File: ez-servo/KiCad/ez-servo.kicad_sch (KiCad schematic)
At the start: 15 parts, among them J1 Driver Pins, J2 SERVO, J3 VSEL, U1 TPS5430DDA

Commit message: fix: add silkscreen markings
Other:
- title: (none) -> EZ Servo
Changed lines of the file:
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@@
 	(generator_version "8.0")
 	(paper "A4")
+	(title_block
+		(title "EZ Servo")
+		(comment 1 "creativecommons.org/licenses/by-sa/4.0/")
+		(comment 2 "License: CC BY-SA 4.0")
+		(comment 3 "Author: Michael Smith")
+	)
 	(junction
 		(at 95.25 143.51)

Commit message: fix: switch feedback resistor footprints for flexibility
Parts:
- R1, R2, R3: footprint Resistor_SMD:R_0805_2012Metric -> Resistor_SMD:R_0805_2012Metric_Pad1.20x1.40mm_HandSolder
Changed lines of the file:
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@@
 			)
 		)
-		(property "Footprint" "Resistor_SMD:R_0805_2012Metric"
+		(property "Footprint" "Resistor_SMD:R_0805_2012Metric_Pad1.20x1.40mm_HandSolder"
 			(at 147.828 124.46 90)
 			(effects
@@
 			)
 		)
-		(property "Footprint" "Resistor_SMD:R_0805_2012Metric"
+		(property "Footprint" "Resistor_SMD:R_0805_2012Metric_Pad1.20x1.40mm_HandSolder"
 			(at 143.002 139.7 90)
 			(effects
@@
 			)
 		)
-		(property "Footprint" "Resistor_SMD:R_0805_2012Metric"
+		(property "Footprint" "Resistor_SMD:R_0805_2012Metric_Pad1.20x1.40mm_HandSolder"
 			(at 156.718 124.46 90)
 			(effects

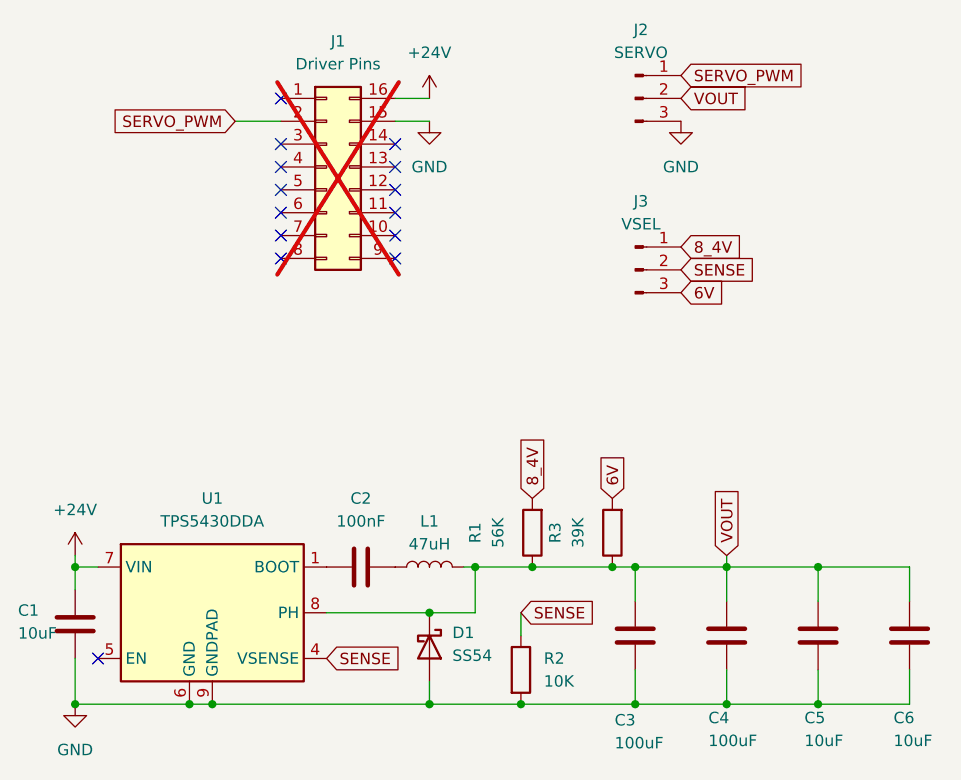
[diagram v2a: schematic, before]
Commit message: feat: add optional servo output through stepper port
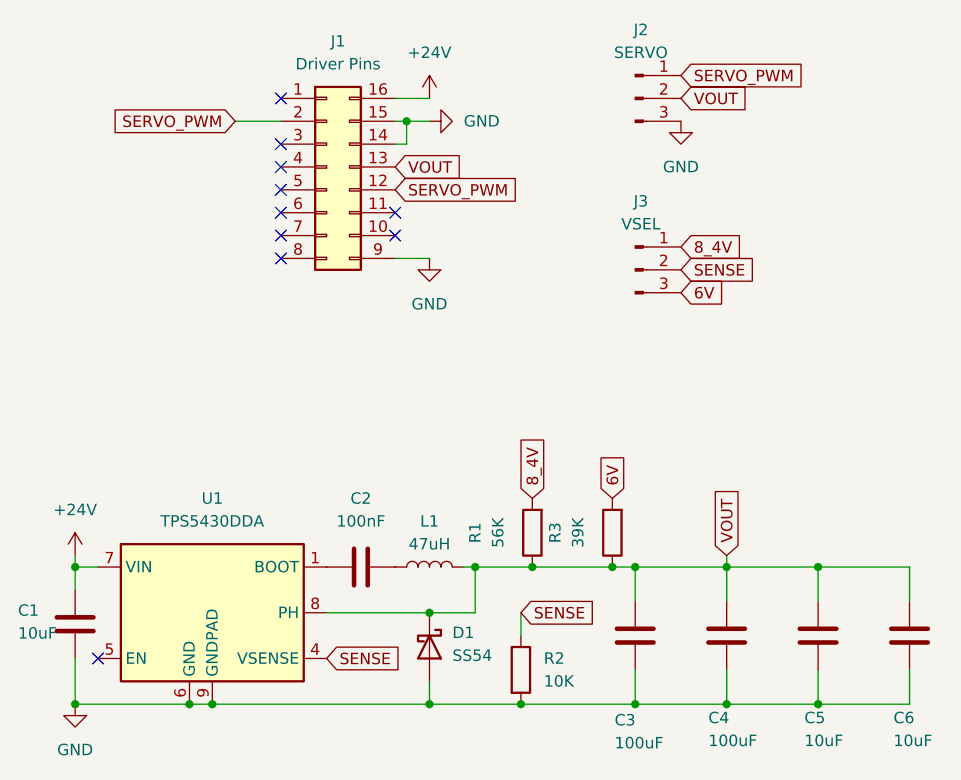
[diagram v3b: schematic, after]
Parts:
- J1: footprint (none) -> Local Library:BTT EZ; now fitted
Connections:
- net GND: now also J1.14 (Pin_14), J1.9 (Pin_9)
- net SERVO_PWM: now also J1.12 (Pin_12)
- net VOUT: now also J1.13 (Pin_13)
- no-connect marks 14 -> 10
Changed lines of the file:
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@@
+	)
+	(junction
+		(at 132.08 78.74)
+		(diameter 0)
+		(color 0 0 0 0)
 	)
 	(junction
@@
 	)
 	(no_connect
-		(at 130.81 83.82)
-	)
-	(no_connect
 		(at 118.11 83.82)
-	)
-	(no_connect
-		(at 130.81 93.98)
 	)
 	(no_connect
@@
 	)
 	(no_connect
-		(at 130.81 81.28)
-	)
-	(no_connect
 		(at 97.79 138.43)
 	)
@@
 	)
 	(no_connect
-		(at 130.81 86.36)
-	)
-	(no_connect
 		(at 118.11 91.44)
 	)
@@
 	(wire
 		(pts
+			(xy 132.08 78.74) (xy 134.62 78.74)
+		)
+		(stroke
+			(width 0)
+			(type default)
+		)
+	)
+	(wire
+		(pts
+			(xy 132.08 81.28) (xy 132.08 78.74)
+		)
+		(stroke
+			(width 0)
+			(type default)
+		)
+	)
+	(wire
+		(pts
 			(xy 95.25 143.51) (xy 107.95 143.51)
 		)
@@
 	(wire
 		(pts
-			(xy 130.81 78.74) (xy 134.62 78.74)
+			(xy 130.81 78.74) (xy 132.08 78.74)
 		)
 		(stroke
@@
 	(wire
 		(pts
+			(xy 130.81 93.98) (xy 134.62 93.98)
+		)
+		(stroke
+			(width 0)
+			(type default)
+		)
+	)
+	(wire
+		(pts
 			(xy 157.48 139.7) (xy 157.48 143.51)
 		)
@@
 	(wire
 		(pts
+			(xy 130.81 81.28) (xy 132.08 81.28)
+		)
+		(stroke
+			(width 0)
+			(type default)
+		)
+	)
+	(wire
+		(pts
 			(xy 95.25 128.27) (xy 95.25 130.81)
 		)
@@
 			(width 0)
 			(type default)
+		)
+	)
+	(global_label "SERVO_PWM"
+		(shape input)
+		(at 130.81 86.36 0)
+		(fields_autoplaced yes)
+		(effects
+			(font
+				(size 1.27 1.27)
+			)
+			(justify left)
+		)
+		(property "Intersheetrefs" "${INTERSHEET_REFS}"
+			(at 144.9832 86.36 0)
+			(effects
+				(font
+					(size 1.27 1.27)
+				)
+				(justify left)
+				(hide yes)
+			)
 		)
 	)
@@
 		(property "Intersheetrefs" "${INTERSHEET_REFS}"
 			(at 154.94 115.3667 90)
+			(effects
+				(font
+					(size 1.27 1.27)
+				)
+				(justify left)
+				(hide yes)
+			)
+		)
+	)
+	(global_label "VOUT"
+		(shape input)
+		(at 130.81 83.82 0)
+		(fields_autoplaced yes)
+		(effects
+			(font
+				(size 1.27 1.27)
+			)
+			(justify left)
+		)
+		(property "Intersheetrefs" "${INTERSHEET_REFS}"
+			(at 138.5124 83.82 0)
 			(effects
 				(font
@@
 		(exclude_from_sim no)
 		(in_bom yes)
-		(on_board no)
-		(dnp yes)
+		(on_board yes)
+		(dnp no)
 		(fields_autoplaced yes)
 		(property "Reference" "J1"
@@
 			)
 		)
-		(property "Footprint" ""
+		(property "Footprint" "Local Library:BTT EZ"
 			(at 123.19 83.82 0)
 			(effects
@@
 	(symbol
 		(lib_id "power:GND")
-		(at 134.62 78.74 0)
+		(at 134.62 78.74 90)
 		(unit 1)
 		(exclude_from_sim no)
@@
 		(fields_autoplaced yes)
 		(property "Reference" "#PWR02"
-			(at 134.62 85.09 0)
+			(at 140.97 78.74 0)
 			(effects
 				(font
@@
 		)
 		(property "Value" "GND"
-			(at 134.62 83.82 0)
-			(effects
-				(font
-					(size 1.27 1.27)
-				)
+			(at 138.43 78.7399 90)
+			(effects
+				(font
+					(size 1.27 1.27)
+				)
+				(justify right)
 			)
 		)
@@
 					(unit 1)
 				)
+			)
+		)
+	)
+	(symbol
+		(lib_id "power:GND")
+		(at 134.62 93.98 0)
+		(unit 1)
+		(exclude_from_sim no)
+		(in_bom yes)
+		(on_board yes)
+		(dnp no)
+		(fields_autoplaced yes)
+		(property "Reference" "#PWR06"
+			(at 134.62 100.33 0)
+			(effects
+				(font
+					(size 1.27 1.27)
+				)
+				(hide yes)
+			)
+		)
+		(property "Value" "GND"
+			(at 134.62 99.06 0)
+			(effects
+				(font
+					(size 1.27 1.27)
+				)
+			)
+		)
+		(property "Footprint" ""
+			(at 134.62 93.98 0)
+			(effects
+				(font
+					(size 1.27 1.27)
+				)
+				(hide yes)
+			)
+		)
+		(property "Datasheet" ""
+			(at 134.62 93.98 0)
+			(effects
+				(font
+					(size 1.27 1.27)
+				)
+				(hide yes)
+			)
+		)
+		(property "Description" "Power symbol creates a global label with name \"GND\" , ground"
+			(at 134.62 93.98 0)
+			(effects
+				(font
+					(size 1.27 1.27)
+				)
+				(hide yes)
+			)
+		)
+		(pin "1"
+		)
+		(instances
+			(project "ez-servo"
+				(path "/d2a470d4-3f75-430d-ade7-9295b060ae03"
+					(reference "#PWR06")
+					(unit 1)
+				)
